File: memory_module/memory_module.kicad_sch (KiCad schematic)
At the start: 174 parts, among them J1 Conn_01x06_Pin, J2 Conn_01x08_Pin, SW1 SW_DIP_x08, SW10 SW_DIP_x08, SW11 SW_DIP_x08, SW12 SW_DIP_x08, SW13 SW_DIP_x08, SW14 SW_DIP_x08, SW15 SW_DIP_x08, SW16 SW_DIP_x08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

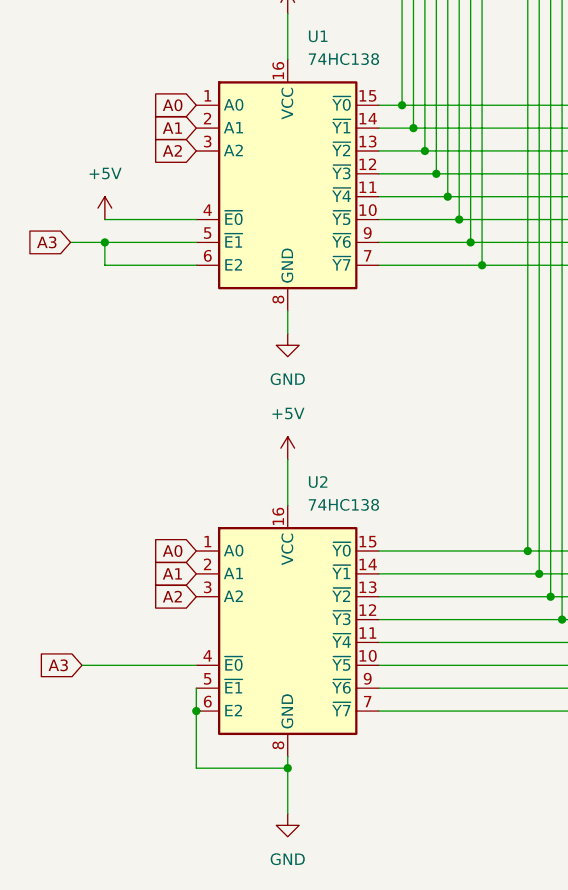
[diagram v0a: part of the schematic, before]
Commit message: 74HC138Nのenableを修正
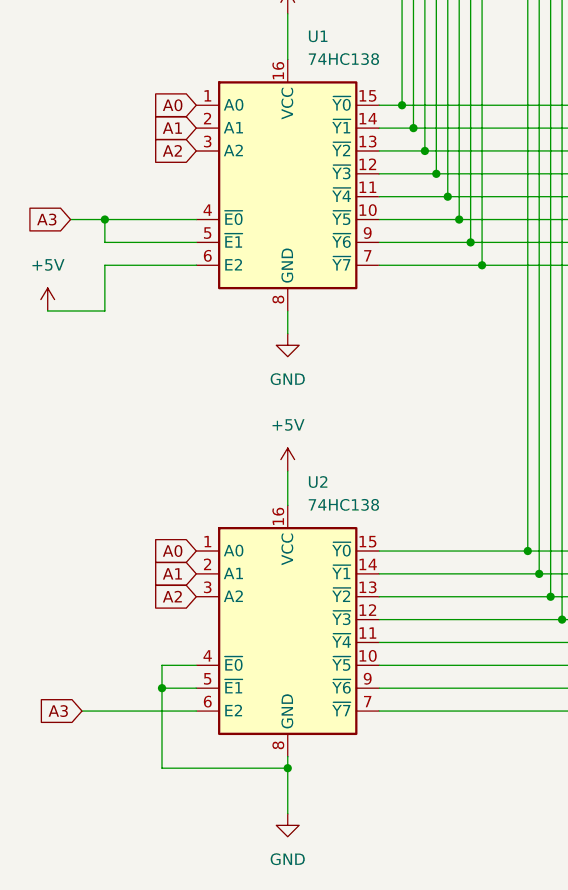
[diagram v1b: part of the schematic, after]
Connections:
- net +5V: now also U1.6 (E2); no longer U1.4 (~{E0})
- net A3: now also U1.4 (~{E0}), U2.6 (E2); no longer U1.6 (E2), U2.4 (~{E0})
- net GND: now also U2.4 (~{E0}); no longer U2.6 (E2)

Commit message: パスコンwip
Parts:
- added C1, C2, C3: 0.1μF, symbol Device:C
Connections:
- net GND is gone; now on net +5V: J1.6 (Pin_6), U1.8 (GND), U2.4 (~{E0}), U2.5 (~{E1}), U2.8 (GND), U3.1 (G1), U3.10 (GND), U3.19 (G2)
- net +5V: now also C1.1, C1.2, C2.1, C2.2, C3.1, C3.2

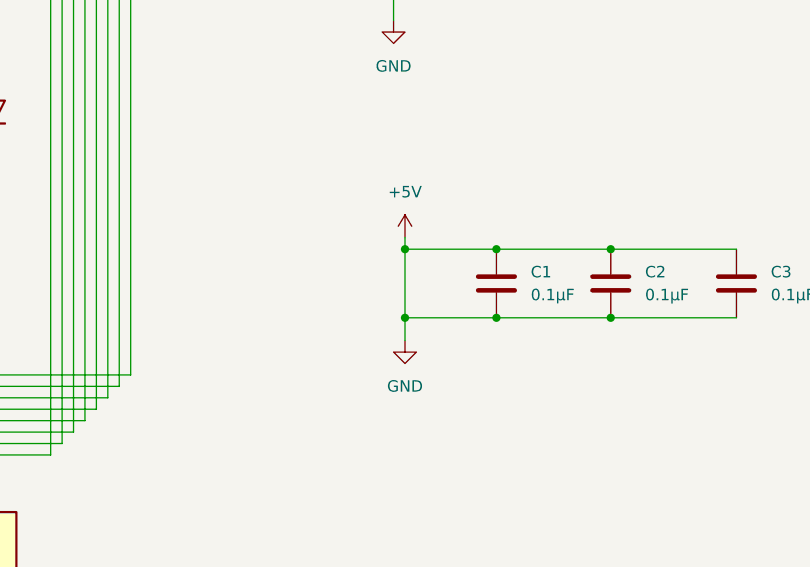
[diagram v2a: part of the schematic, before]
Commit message: パスコン追加
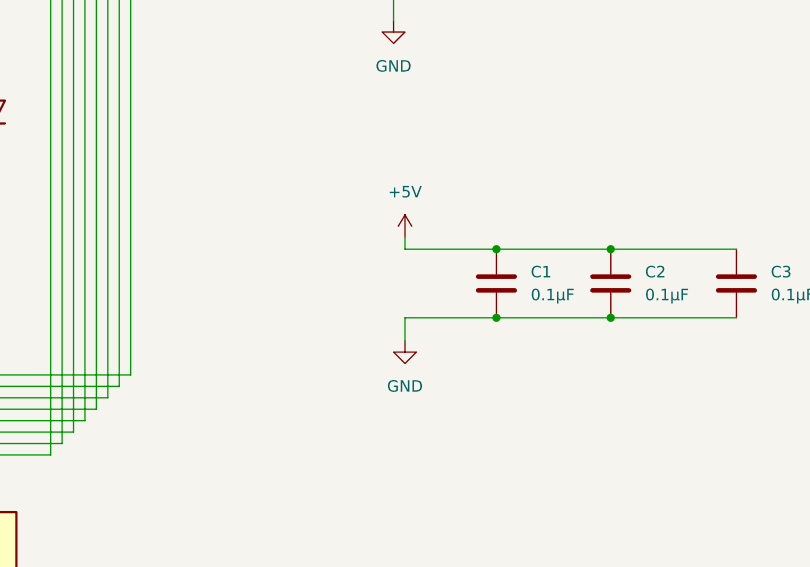
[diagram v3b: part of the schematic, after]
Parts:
- C1, C2, C3: footprint (none) -> Capacitor_THT:C_Disc_D4.3mm_W1.9mm_P5.00mm
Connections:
- net +5V: no longer C1.2, C2.2, C3.2, J1.6 (Pin_6), U1.8 (GND), U2.4 (~{E0}), U2.5 (~{E1}), U2.8 (GND), U3.1 (G1), U3.10 (GND), U3.19 (G2)
- new net GND: C1.2, C2.2, C3.2, J1.6 (Pin_6), U1.8 (GND), U2.4 (~{E0}), U2.5 (~{E1}), U2.8 (GND), U3.1 (G1), U3.10 (GND), U3.19 (G2)
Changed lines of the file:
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@@
 	)
 	(junction
-		(at 349.25 111.76)
-		(diameter 0)
-		(color 0 0 0 0)
-	)
-	(junction
 		(at 182.88 55.88)
 		(diameter 0)
@@
 	)
 	(junction
-		(at 349.25 119.38)
-		(diameter 0)
-		(color 0 0 0 0)
-	)
-	(junction
 		(at 119.38 132.08)
 		(diameter 0)
@@
 	(wire
 		(pts
-			(xy 349.25 111.76) (xy 349.25 119.38)
-		)
-		(stroke
-			(width 0)
-			(type default)
-		)
-	)
-	(wire
-		(pts
 			(xy 175.26 100.33) (xy 175.26 107.95)
 		)
@@
 			)
 		)
-		(property "Footprint" ""
+		(property "Footprint" "Capacitor_THT:C_Disc_D4.3mm_W1.9mm_P5.00mm"
 			(at 387.0452 119.38 0)
 			(effects
@@
 			)
 		)
-		(property "Footprint" ""
+		(property "Footprint" "Capacitor_THT:C_Disc_D4.3mm_W1.9mm_P5.00mm"
 			(at 360.3752 119.38 0)
 			(effects
@@
 			)
 		)
-		(property "Footprint" ""
+		(property "Footprint" "Capacitor_THT:C_Disc_D4.3mm_W1.9mm_P5.00mm"
 			(at 373.0752 119.38 0)
 			(effects
